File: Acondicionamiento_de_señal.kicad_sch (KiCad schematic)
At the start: 31 parts, among them U2 TL074

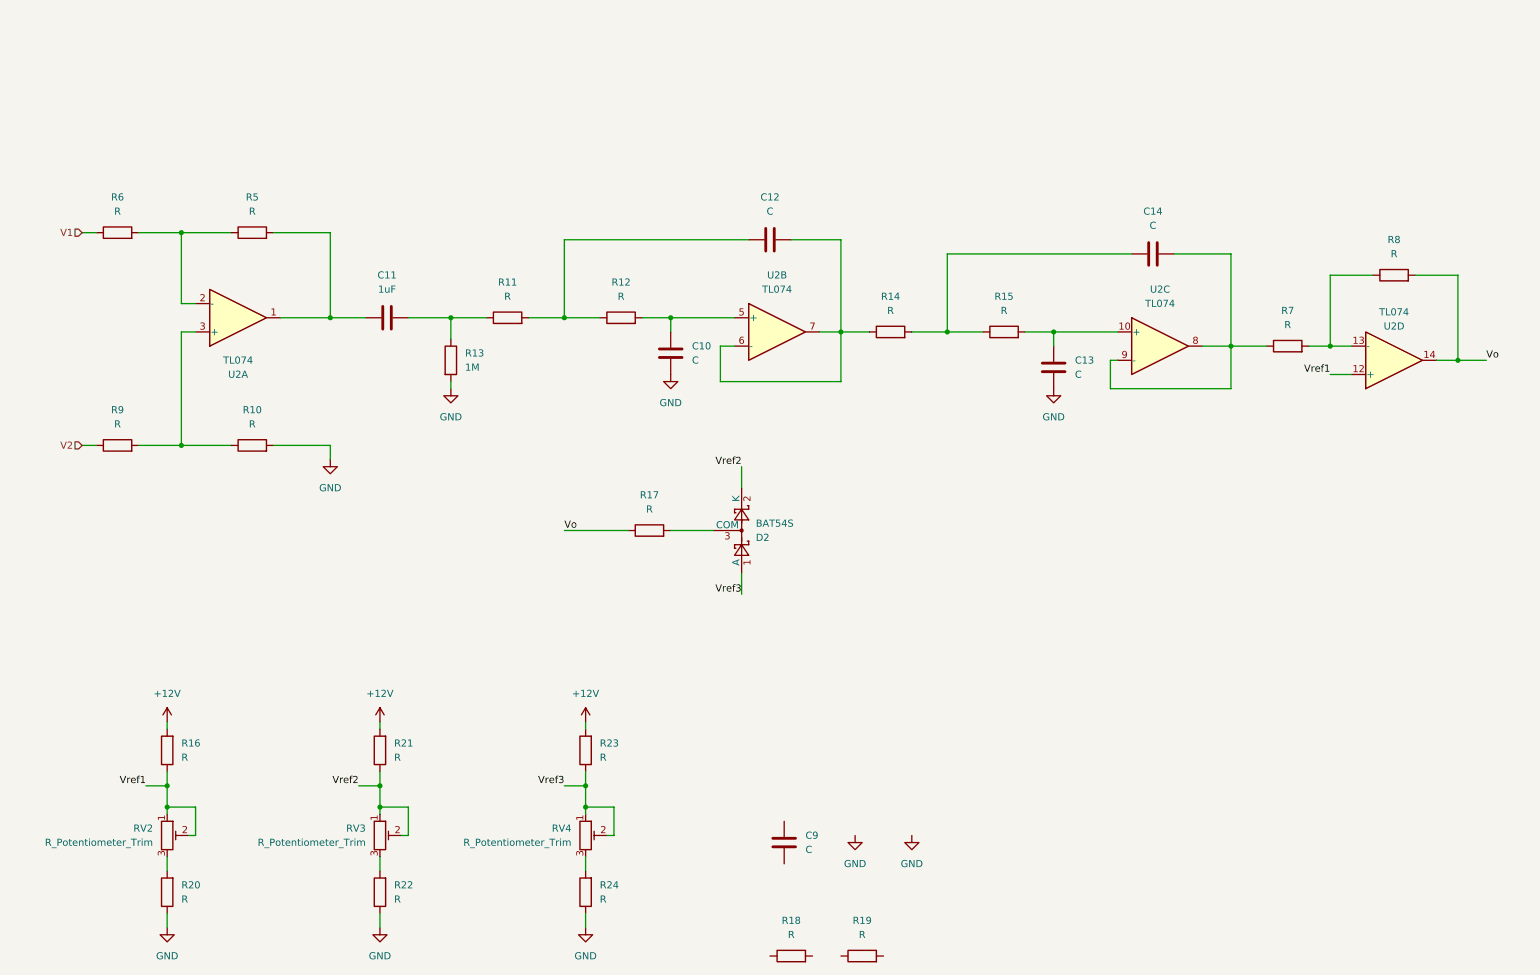
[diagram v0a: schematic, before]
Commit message: Update schematics: signal conditioning, power, ESP32-S3, output, and add signal measurement sub-sheet
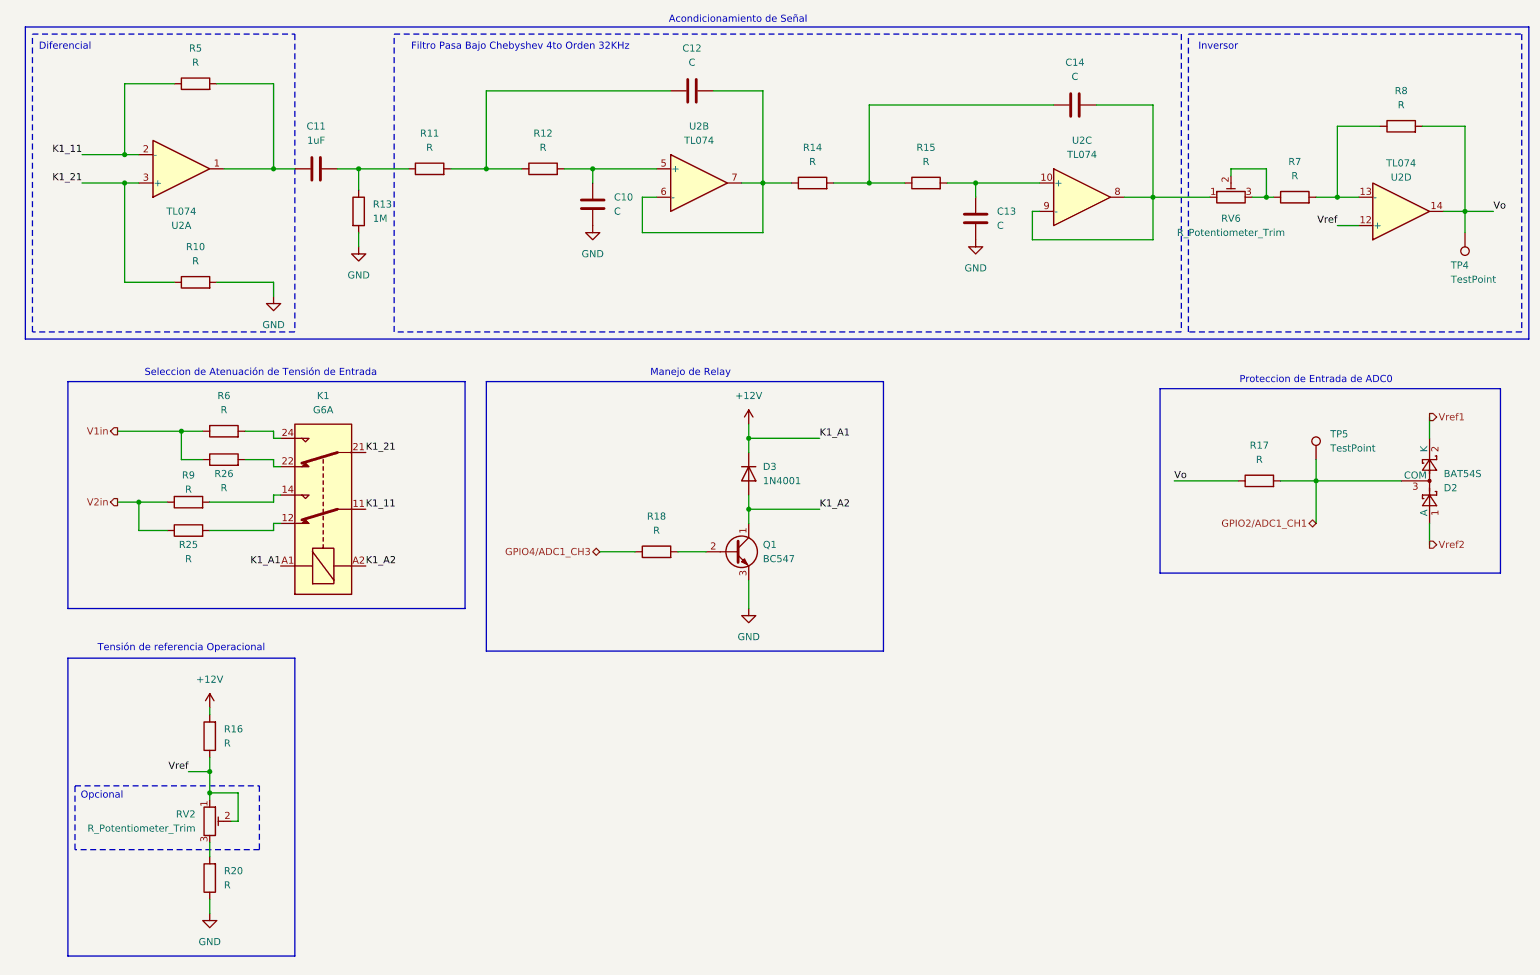
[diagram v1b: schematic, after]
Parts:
- removed C9: C, symbol Device:C
- removed R19, R21, R22, R23, R24: R, symbol Device:R
- removed RV3, RV4: R_Potentiometer_Trim, Potentiometer_THT:Potentiometer_Bourns_3266Y_Vertical, symbol Device:R_Potentiometer_Trim
- added D3: 1N4001, Diode_THT:D_DO-41_SOD81_P10.16mm_Horizontal, symbol Diode:1N4001
- added K1: G6A, Relay_THT:Relay_DPDT_Omron_G6A, symbol Relay:G6A
- added Q1: BC547, Package_TO_SOT_THT:TO-92_Inline, symbol Transistor_BJT:BC547
- added R25, R26: R, Resistor_THT:R_Axial_DIN0207_L6.3mm_D2.5mm_P10.16mm_Horizontal, symbol Device:R
- added RV6: R_Potentiometer_Trim, Potentiometer_THT:Potentiometer_Bourns_3266Y_Vertical, symbol Device:R_Potentiometer_Trim
- added TP4, TP5: TestPoint, TestPoint:TestPoint_Loop_D2.50mm_Drill1.0mm, symbol Connector:TestPoint
- C10, C11, C12, C13, C14: footprint (none) -> Capacitor_THT:C_Disc_D7.5mm_W2.5mm_P5.00mm
- R10, R11, R12, R13, R14, R15, R16, R17, R18, R20, R5, R6, R7, R8, R9: footprint (none) -> Resistor_THT:R_Axial_DIN0207_L6.3mm_D2.5mm_P10.16mm_Horizontal
- U2: footprint (none) -> Package_DIP:CERDIP-14_W7.62mm_SideBrazed_LongPads_Socket
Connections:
- net Vref3 is gone; now on net Vref2: D2.1 (A)
- net +12V: now also D3.1 (K), K1.A1
- net GND: now also Q1.3 (E)
- net Vo: now also TP4.1
- net Vref1: now also D2.2 (K); no longer R16.1, RV2.1, RV2.2, U2.12 (+)
- net Vref2: no longer D2.2 (K)
- net at C14.2, U2.8, U2.9 (-): now also RV6.1; no longer R7.1
- net K1_21: now reaches R10.1, U2.3 (+)
- net K1_21: now also K1.21; no longer R9.2
- net K1_11: now reaches R5.1, U2.2 (-)
- net K1_11: now also K1.11; no longer R6.2
- net GPIO2/ADC1_CH1: now reaches D2.3 (COM), R17.2
- net GPIO2/ADC1_CH1: now also TP5.1
- net GPIO4/ADC1_CH3: now reaches R18.1
- net at R18.2: now also Q1.2 (B)
- net V1 renamed V1in
- net V1in: now also R26.1
- net V2 renamed V2in
- net V2in: now also R25.1
- new net: K1.14, R9.2
- new net: K1.24, R6.2
- new net: K1.22, R26.2
- new net: K1.12, R25.2
- new net: R7.1, RV6.2, RV6.3
- new net K1_A2: D3.2 (A), K1.A2, Q1.1 (C)
- new net Vref: R16.1, RV2.1, RV2.2, U2.12 (+)
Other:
- note added: "Acondicionamiento de Señal"
- note added: "Diferencial"
- note added: "Filtro Pasa Bajo Chebyshev 4to Orden 32KHz"
- note added: "Inversor"
- note added: "Manejo de Relay"
- note added: "Opcional"
- note added: "Proteccion de Entrada de ADC0"
- note added: "Seleccion de Atenuación de Tensión de Entrada"
- note added: "Tensión de referencia Operacional"
- moved on the sheet: C10, C11, C12, C13, C14, D2, R10, R11, R12, R13, R14, R15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

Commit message: Save local schematic and board updates before 3D model path resolution
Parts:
- Q1: footprint Package_TO_SOT_THT:TO-92_Inline -> Package_TO_SOT_THT:TO-92_HandSolder
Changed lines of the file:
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@@
 			)
 		)
-		(property "Footprint" "Package_TO_SOT_THT:TO-92_Inline"
+		(property "Footprint" "Package_TO_SOT_THT:TO-92_HandSolder"
 			(at 146.05 121.285 0)
 			(hide yes)
